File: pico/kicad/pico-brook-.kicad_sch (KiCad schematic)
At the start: 15 parts, among them J10 Conn_01x03_Male, J11 Conn_01x04_Female, J2 Conn_01x05_Male, J3 Screw_Terminal_01x20, J4 Conn_01x04_Male, J5 Conn_01x05_Male, J6 Conn_01x04_Male, J7 Conn_01x04_Male, J8 Conn_01x04_Male, J9 Conn_02x10_Odd_Even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

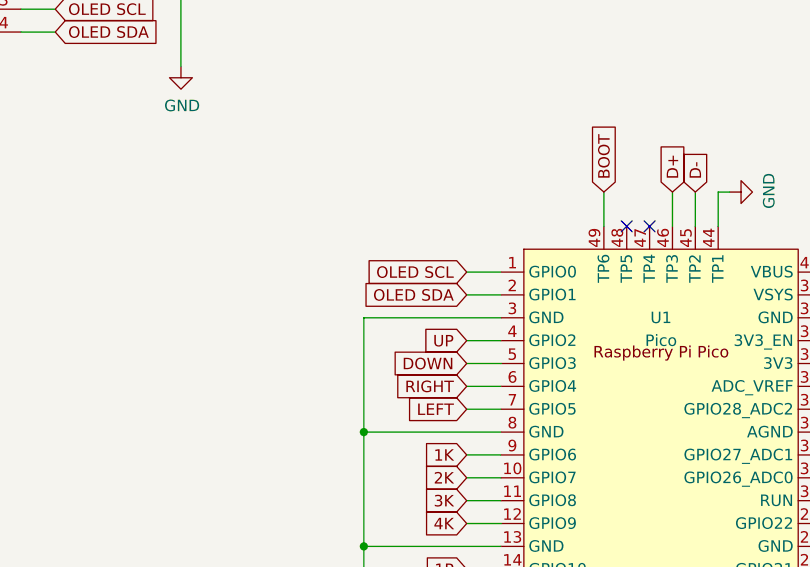
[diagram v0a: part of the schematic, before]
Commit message: Swap OLED SDA and OLED SCL pins and headers on PCB and Schematic
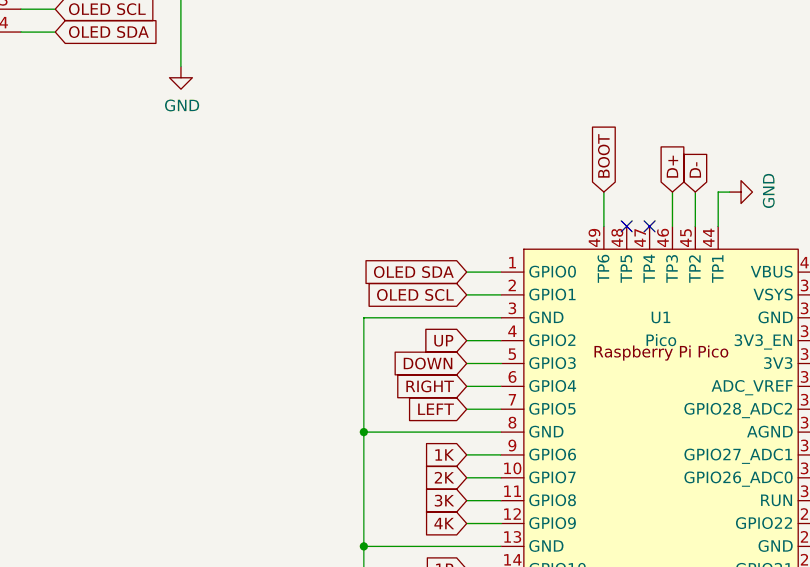
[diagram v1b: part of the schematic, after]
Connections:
- net OLED SCL: now also U1.2 (GPIO1); no longer U1.1 (GPIO0)
- net OLED SDA: now also U1.1 (GPIO0); no longer U1.2 (GPIO1)
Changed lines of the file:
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@@
-    )
-  )
-  (global_label "OLED SCL" (shape input) (at 166.37 95.25 180) (fields_autoplaced)
-    (effects (font (size 1.27 1.27)) (justify right))
-    (property "Intersheet References" "${INTERSHEET_REFS}" (id 0) (at 154.7929 95.1706 0)
-      (effects (font (size 1.27 1.27)) (justify right) hide)
     )
   )
@@
     )
   )
-  (global_label "OLED SDA" (shape input) (at 166.37 97.79 180) (fields_autoplaced)
-    (effects (font (size 1.27 1.27)) (justify right))
-    (property "Intersheet References" "${INTERSHEET_REFS}" (id 0) (at 154.7325 97.7106 0)
-      (effects (font (size 1.27 1.27)) (justify right) hide)
-    )
-  )
   (global_label "1K" (shape input) (at 166.37 115.57 180) (fields_autoplaced)
     (effects (font (size 1.27 1.27)) (justify right))
@@
     )
   )
+  (global_label "OLED SCL" (shape input) (at 166.37 97.79 180) (fields_autoplaced)
+    (effects (font (size 1.27 1.27)) (justify right))
+    (property "Intersheet References" "${INTERSHEET_REFS}" (id 0) (at 154.7929 97.7106 0)
+      (effects (font (size 1.27 1.27)) (justify right) hide)
+    )
+  )
   (global_label "RIGHT" (shape input) (at 55.88 57.15 0) (fields_autoplaced)
     (effects (font (size 1.27 1.27)) (justify left))
@@
       (effects (font (size 1.27 1.27)) (justify right) hide)
     )
+  )
+  (global_label "OLED SDA" (shape input) (at 166.37 95.25 180) (fields_autoplaced)
+    (effects (font (size 1.27 1.27)) (justify right))
+    (property "Intersheet References" "${INTERSHEET_REFS}" (id 0) (at 154.7325 95.1706 0)
+      (effects (font (size 1.27 1.27)) (justify right) hide)
+    )

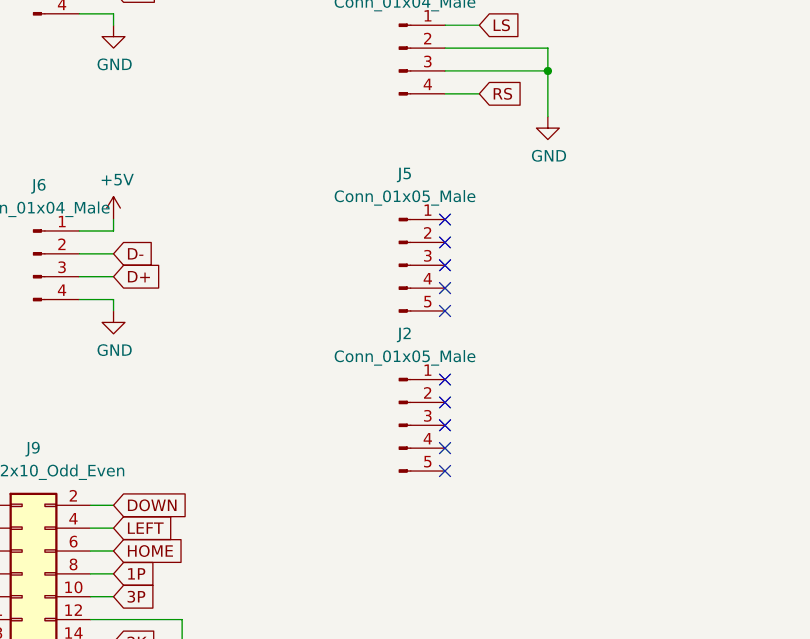
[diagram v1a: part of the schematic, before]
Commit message: Minor adjustments to traces, remove J2 and J5 due to nonuse
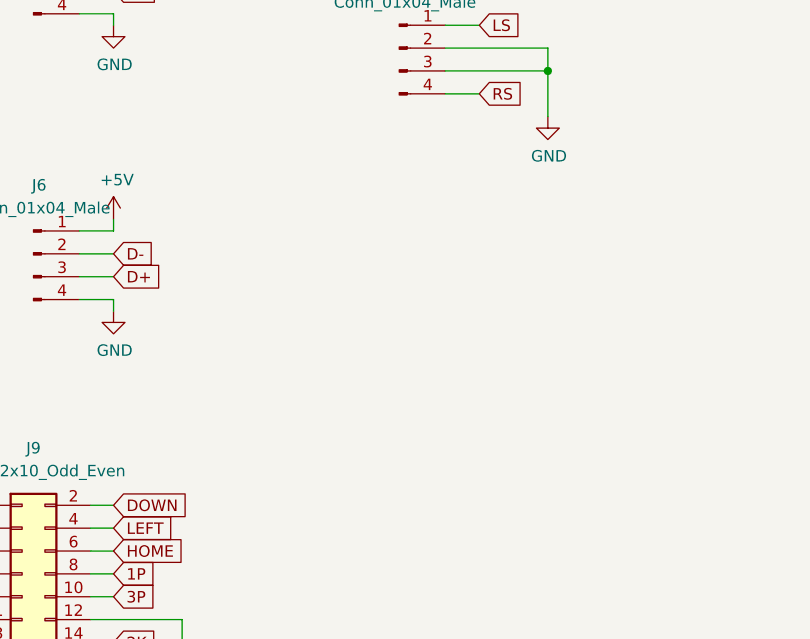
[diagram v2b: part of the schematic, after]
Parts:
- removed J2, J5: Conn_01x05_Male, Connector_PinHeader_2.00mm:PinHeader_1x05_P2.00mm_Vertical, symbol Connector:Conn_01x05_Male
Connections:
- no-connect marks 19 -> 9
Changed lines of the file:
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@@
   (no_connect (at 186.69 90.17))
   (no_connect (at 205.74 123.19))
-  (no_connect (at 92.71 146.05))
-  (no_connect (at 92.71 138.43))
-  (no_connect (at 92.71 140.97))
-  (no_connect (at 92.71 143.51))
-  (no_connect (at 92.71 166.37))
-  (no_connect (at 92.71 148.59))
-  (no_connect (at 92.71 156.21))
-  (no_connect (at 92.71 158.75))
-  (no_connect (at 92.71 161.29))
-  (no_connect (at 92.71 163.83))
   (no_connect (at 205.74 113.03))
   (no_connect (at 205.74 102.87))
@@
     (pin "1")
   )
-  (symbol (lib_id "Connector:Conn_01x05_Male") (at 87.63 143.51 0) (unit 1)
-    (in_bom yes) (on_board yes) (fields_autoplaced)
-    (property "Reference" "J5" (id 0) (at 88.265 133.35 0))
-    (property "Value" "Conn_01x05_Male" (id 1) (at 88.265 135.89 0))
-    (property "Footprint" "Connector_PinHeader_2.00mm:PinHeader_1x05_P2.00mm_Vertical" (id 2) (at 87.63 143.51 0)
-      (effects (font (size 1.27 1.27)) hide)
-    )
-    (property "Datasheet" "~" (id 3) (at 87.63 143.51 0)
-      (effects (font (size 1.27 1.27)) hide)
-    )
-    (pin "1")
-    (pin "2")
-    (pin "3")
-    (pin "4")
-    (pin "5")
-  )
   (symbol (lib_id "power:GND") (at 220.98 149.86 0) (unit 1)
     (in_bom yes) (on_board yes)
@@
     (pin "4")
   )
-  (symbol (lib_id "Connector:Conn_01x05_Male") (at 87.63 161.29 0) (unit 1)
-    (in_bom yes) (on_board yes) (fields_autoplaced)
-    (property "Reference" "J2" (id 0) (at 88.265 151.13 0))
-    (property "Value" "Conn_01x05_Male" (id 1) (at 88.265 153.67 0))
-    (property "Footprint" "Connector_PinHeader_2.00mm:PinHeader_1x05_P2.00mm_Vertical" (id 2) (at 87.63 161.29 0)
-      (effects (font (size 1.27 1.27)) hide)
-    )
-    (property "Datasheet" "~" (id 3) (at 87.63 161.29 0)
-      (effects (font (size 1.27 1.27)) hide)
-    )
-    (pin "1")
-    (pin "2")
-    (pin "3")
-    (pin "4")
-    (pin "5")
-  )
   (symbol (lib_id "power:+5V") (at 55.88 138.43 0) (unit 1)
     (in_bom yes) (on_board yes)
@@
       (reference "H4") (unit 1) (value "MountingHole") (footprint "MountingHole:MountingHole_3.2mm_M3")
     )
-    (path "/a6d50896-f15e-45b0-81f6-d53b078764b2"
-      (reference "J2") (unit 1) (value "Conn_01x05_Male") (footprint "Connector_PinHeader_2.00mm:PinHeader_1x05_P2.00mm_Vertical")
-    )
     (path "/d18c544f-661a-495a-9d4f-ca9214eda290"
       (reference "J3") (unit 1) (value "Screw_Terminal_01x20") (footprint "Connector_Wago:Wago_734-150_1x20_P3.50mm_Vertical")
@@
       (reference "J4") (unit 1) (value "Conn_01x04_Male") (footprint "Connector_PinSocket_2.00mm:PinSocket_1x04_P2.00mm_Vertical")
     )
-    (path "/51e77ea7-ff52-4a5d-ada1-d961b6ef7642"
-      (reference "J5") (unit 1) (value "Conn_01x05_Male") (footprint "Connector_PinHeader_2.00mm:PinHeader_1x05_P2.00mm_Vertical")
-    )
     (path "/a220aa7e-8cad-45f5-a4bc-72eb7d34202c"
